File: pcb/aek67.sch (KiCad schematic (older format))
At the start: 20 parts, among them J1 AVR-ISP-6, SW1 SW_PUSH, U1 ATmega32U4-AU, U2 PRTR5V0U2X, X1 XTAL_GND

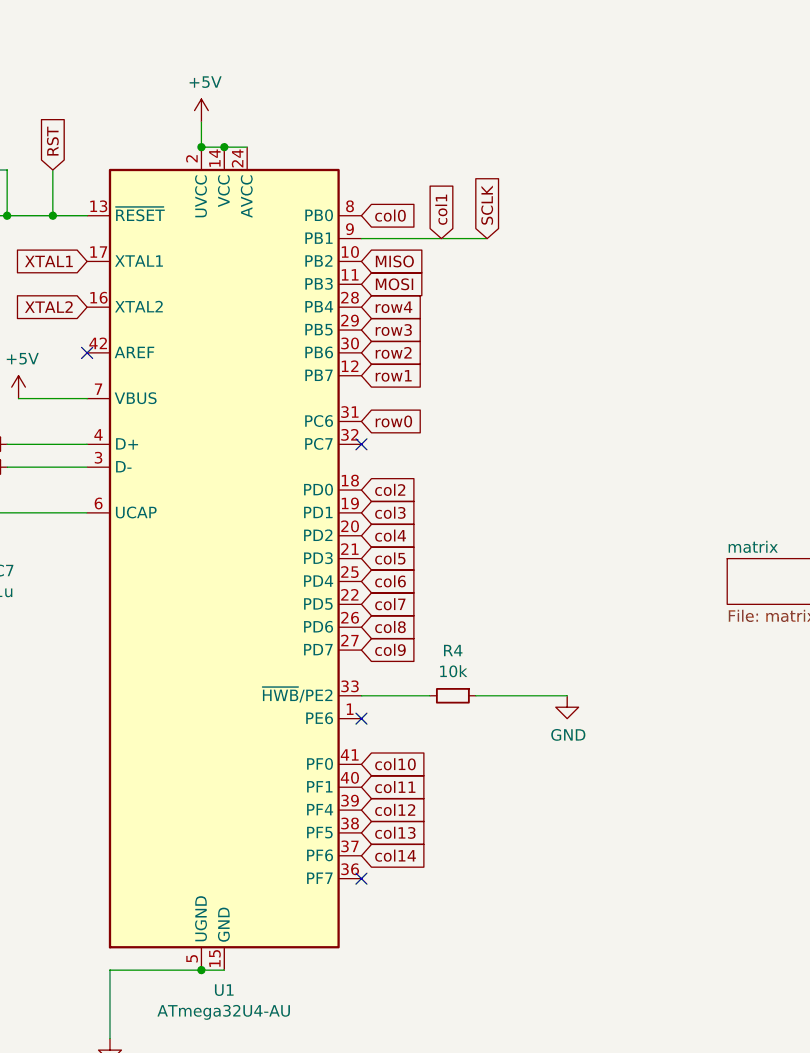
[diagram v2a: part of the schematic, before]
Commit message: reorder rows/cols to MCU pins
to better orient them
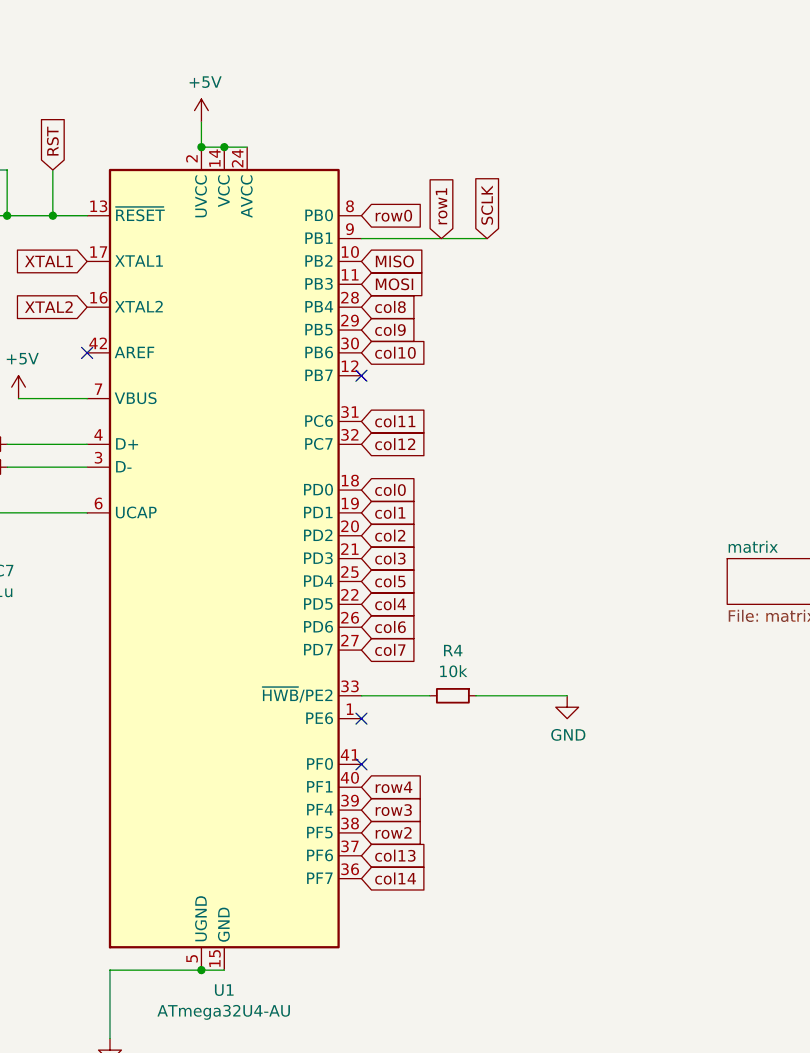
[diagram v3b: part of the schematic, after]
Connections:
- net col0: now also U1.18 (PD0); no longer U1.8 (PB0)
- net col10: now also U1.30 (PB6); no longer U1.41 (PF0)
- net col11: now also U1.31 (PC6); no longer U1.40 (PF1)
- net col12: now also U1.32 (PC7); no longer U1.39 (PF4)
- net col13: now also U1.37 (PF6); no longer U1.38 (PF5)
- net col14: now also U1.36 (PF7); no longer U1.37 (PF6)
- net col2: now also U1.20 (PD2); no longer U1.18 (PD0)
- net col3: now also U1.21 (PD3); no longer U1.19 (PD1)
- net col4: now also U1.22 (PD5); no longer U1.20 (PD2)
- net col5: now also U1.25 (PD4); no longer U1.21 (PD3)
- net col6: now also U1.26 (PD6); no longer U1.25 (PD4)
- net col7: now also U1.27 (PD7); no longer U1.22 (PD5)
- net col8: now also U1.28 (PB4); no longer U1.26 (PD6)
- net col9: now also U1.29 (PB5); no longer U1.27 (PD7)
- net row0: now also U1.8 (PB0); no longer U1.31 (PC6)
- net row2: now also U1.38 (PF5); no longer U1.30 (PB6)
- net row3: now also U1.39 (PF4); no longer U1.29 (PB5)
- net row4: now also U1.40 (PF1); no longer U1.28 (PB4)
- net row1: no longer names the net of U1.12 (PB7)
- new net col1: U1.19 (PD1)
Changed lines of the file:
@@
 $EndSheet
 Text GLabel 7100 3600 2    50   Input ~ 0
+col11
+Text GLabel 7100 3300 2    50   Input ~ 0
+col10
+Text GLabel 7100 3200 2    50   Input ~ 0
+col9
+Text GLabel 7100 3100 2    50   Input ~ 0
+col8
+Text GLabel 7100 3900 2    50   Input ~ 0
+col0
+Text GLabel 7100 4000 2    50   Input ~ 0
+col1
+Text GLabel 7100 4100 2    50   Input ~ 0
+col2
+Text GLabel 7100 4200 2    50   Input ~ 0
+col3
+Text GLabel 7100 4300 2    50   Input ~ 0
+col5
+Text GLabel 7100 4400 2    50   Input ~ 0
+col4
+Text GLabel 7100 4500 2    50   Input ~ 0
+col6
+Text GLabel 7100 4600 2    50   Input ~ 0
+col7
+Text GLabel 7100 5200 2    50   Input ~ 0
+row4
+Text GLabel 7100 5300 2    50   Input ~ 0
+row3
+Text GLabel 7100 5400 2    50   Input ~ 0
+row2
+Text GLabel 7100 5500 2    50   Input ~ 0
+col13
+Text GLabel 7100 2700 2    50   Input ~ 0
 row0
-Text GLabel 7100 3400 2    50   Input ~ 0
-row1
-Text GLabel 7100 3300 2    50   Input ~ 0
-row2
-Text GLabel 7100 3200 2    50   Input ~ 0
-row3
-Text GLabel 7100 3100 2    50   Input ~ 0
-row4
-Text GLabel 7100 3900 2    50   Input ~ 0
-col2
-Text GLabel 7100 4000 2    50   Input ~ 0
-col3
-Text GLabel 7100 4100 2    50   Input ~ 0
-col4
-Text GLabel 7100 4200 2    50   Input ~ 0
-col5
-Text GLabel 7100 4300 2    50   Input ~ 0
-col6
-Text GLabel 7100 4400 2    50   Input ~ 0
-col7
-Text GLabel 7100 4500 2    50   Input ~ 0
-col8
-Text GLabel 7100 4600 2    50   Input ~ 0
-col9
-Text GLabel 7100 5100 2    50   Input ~ 0
-col10
-Text GLabel 7100 5200 2    50   Input ~ 0
-col11
-Text GLabel 7100 5300 2    50   Input ~ 0
-col12
-Text GLabel 7100 5400 2    50   Input ~ 0
-col13
-Text GLabel 7100 5500 2    50   Input ~ 0
-col14
-Text GLabel 7100 2700 2    50   Input ~ 0
-col0
 Wire Wire Line
 	7100 2800 7650 2800
 Text GLabel 7450 2800 1    50   Input ~ 0
-col1
-NoConn ~ 7100 5600
+row1
 NoConn ~ 7100 4900
-NoConn ~ 7100 3700
 $Comp
 L power:GND #PWR09
@@
 	2500 6650 2500 6750
 Connection ~ 2500 6650
+Text GLabel 7100 3700 2    50   Input ~ 0
+col12
+Text GLabel 7100 5600 2    50   Input ~ 0
+col14
+NoConn ~ 7100 5100
+NoConn ~ 7100 3400
 $EndSCHEMATC

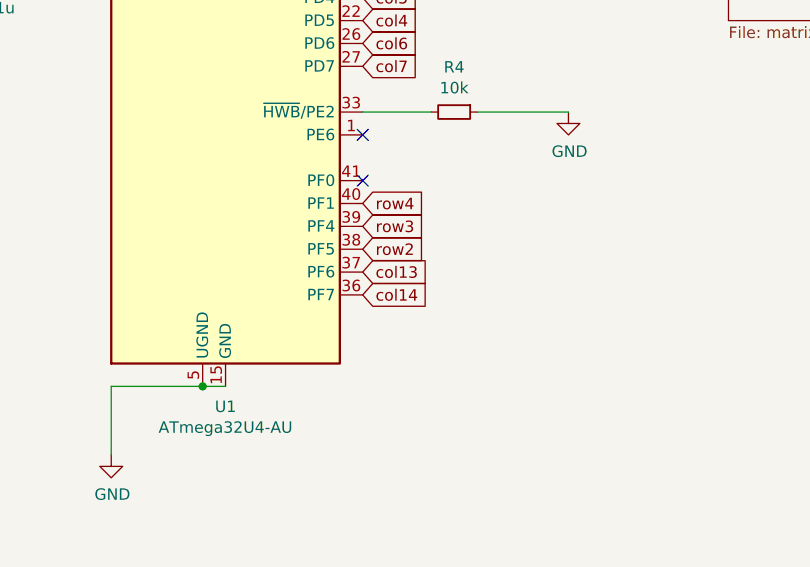
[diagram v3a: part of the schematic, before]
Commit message: routed almost all rows& columns
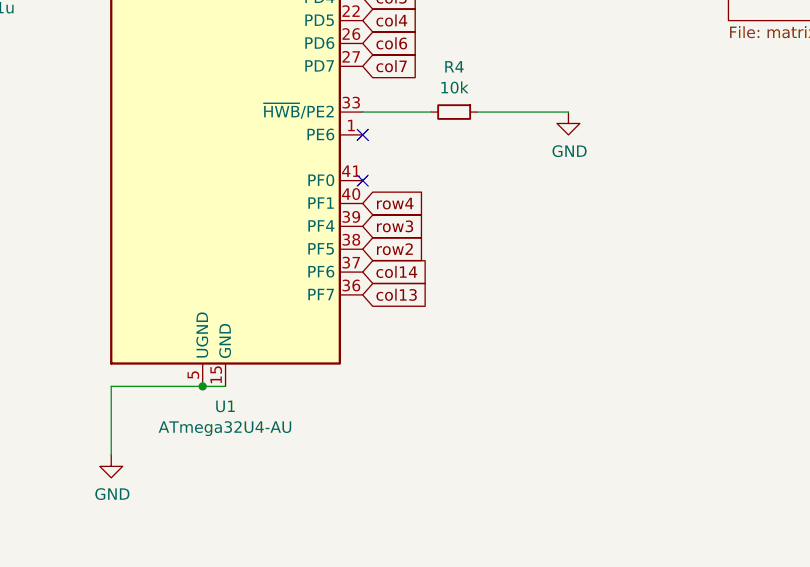
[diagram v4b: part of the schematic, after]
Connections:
- net col13: now also U1.36 (PF7); no longer U1.37 (PF6)
- net col14: now also U1.37 (PF6); no longer U1.36 (PF7)
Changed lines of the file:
@@
 row2
 Text GLabel 7100 5500 2    50   Input ~ 0
-col13
+col14
 Text GLabel 7100 2700 2    50   Input ~ 0
 row0
@@
 col12
 Text GLabel 7100 5600 2    50   Input ~ 0
-col14
+col13
 NoConn ~ 7100 5100
 NoConn ~ 7100 3400

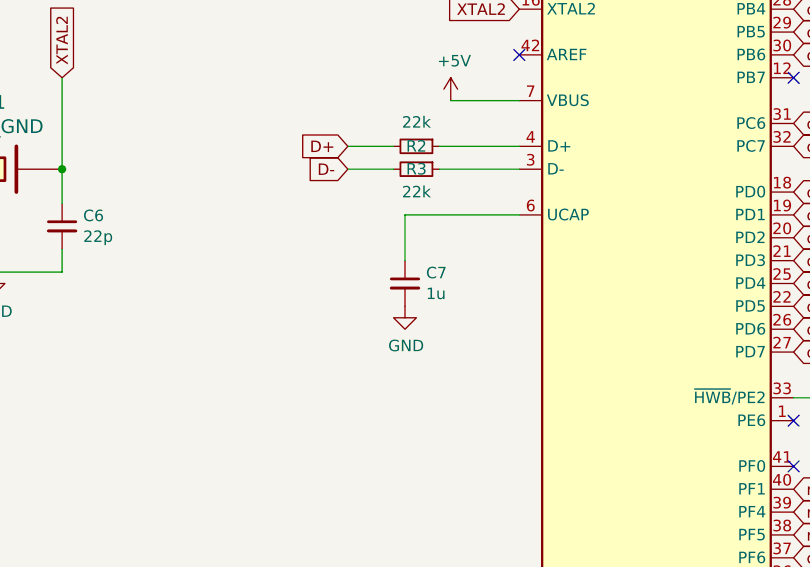
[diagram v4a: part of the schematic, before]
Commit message: Fix footprints of Capacitors
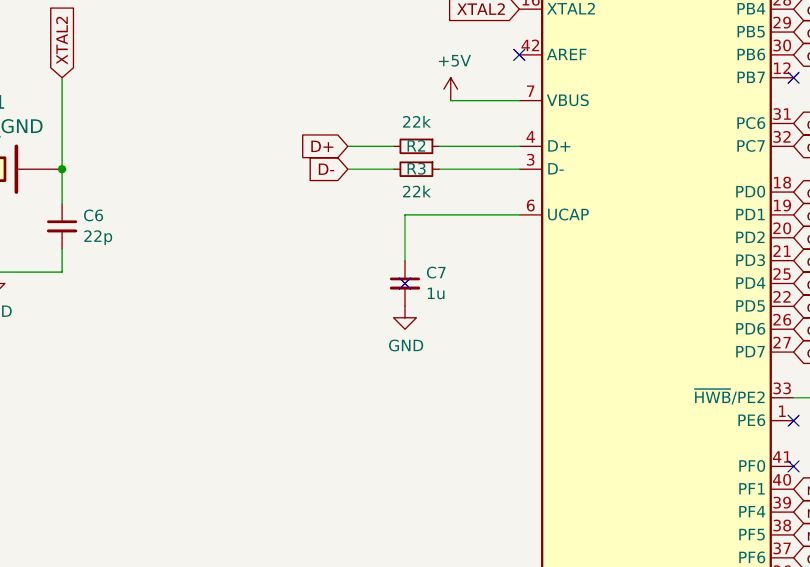
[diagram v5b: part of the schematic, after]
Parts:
- C1, C2, C3, C4, C5, C6, C7: footprint Diode_SMD:D_SOD-123 -> Capacitor_SMD:C_0805_2012Metric_Pad1.15x1.40mm_HandSolder
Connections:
- no-connect marks 6 -> 7
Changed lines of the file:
@@
 F 0 "C1" H 750 1150 50  0000 L CNN
 F 1 "0.1u" H 650 1000 50  0000 L CNN
-F 2 "Diode_SMD:D_SOD-123" H 900 1100 50  0001 C CNN
+F 2 "Capacitor_SMD:C_0805_2012Metric_Pad1.15x1.40mm_HandSolder" H 900 1100 50  0001 C CNN
 F 3 "~" H 900 1100 50  0001 C CNN
 	1    900  1100
@@
 F 0 "C2" H 1050 1150 50  0000 L CNN
 F 1 "0.1u" H 950 1000 50  0000 L CNN
-F 2 "Diode_SMD:D_SOD-123" H 1200 1100 50  0001 C CNN
+F 2 "Capacitor_SMD:C_0805_2012Metric_Pad1.15x1.40mm_HandSolder" H 1200 1100 50  0001 C CNN
 F 3 "~" H 1200 1100 50  0001 C CNN
 	1    1200 1100
@@
 F 0 "C3" H 1650 1150 50  0000 L CNN
 F 1 "0.1u" H 1600 1000 50  0000 L CNN
-F 2 "Diode_SMD:D_SOD-123" H 1600 1100 50  0001 C CNN
+F 2 "Capacitor_SMD:C_0805_2012Metric_Pad1.15x1.40mm_HandSolder" H 1600 1100 50  0001 C CNN
 F 3 "~" H 1600 1100 50  0001 C CNN
 	1    1600 1100
@@
 F 0 "C4" H 1950 1150 50  0000 L CNN
 F 1 "10u" H 1900 1000 50  0000 L CNN
-F 2 "Diode_SMD:D_SOD-123" H 1900 1100 50  0001 C CNN
+F 2 "Capacitor_SMD:C_0805_2012Metric_Pad1.15x1.40mm_HandSolder" H 1900 1100 50  0001 C CNN
 F 3 "~" H 1900 1100 50  0001 C CNN
 	1    1900 1100
@@
 F 0 "C5" H 3100 4100 50  0000 L CNN
 F 1 "22p" H 3100 4000 50  0000 L CNN
-F 2 "Diode_SMD:D_SOD-123" H 3300 4050 50  0001 C CNN
+F 2 "Capacitor_SMD:C_0805_2012Metric_Pad1.15x1.40mm_HandSolder" H 3300 4050 50  0001 C CNN
 F 3 "~" H 3300 4050 50  0001 C CNN
 	1    3300 4050
@@
 F 0 "C6" H 3992 4096 50  0000 L CNN
 F 1 "22p" H 3992 4005 50  0000 L CNN
-F 2 "Diode_SMD:D_SOD-123" H 3900 4050 50  0001 C CNN
+F 2 "Capacitor_SMD:C_0805_2012Metric_Pad1.15x1.40mm_HandSolder" H 3900 4050 50  0001 C CNN
 F 3 "~" H 3900 4050 50  0001 C CNN
 	1    3900 4050
@@
 F 0 "C7" H 5492 4346 50  0000 L CNN
 F 1 "1u" H 5492 4255 50  0000 L CNN
-F 2 "Diode_SMD:D_SOD-123" H 5400 4300 50  0001 C CNN
+F 2 "Capacitor_SMD:C_0805_2012Metric_Pad1.15x1.40mm_HandSolder" H 5400 4300 50  0001 C CNN
 F 3 "~" H 5400 4300 50  0001 C CNN
 	1    5400 4300
@@
 NoConn ~ 7100 5100
 NoConn ~ 7100 3400
+NoConn ~ 5400 4300
 $EndSCHEMATC

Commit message: use the correct crystal footprints
with opposite XTAL pads, in consequence redid the GND zones
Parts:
- X1: symbol keyboard_parts:XTAL_GND -> Device:Crystal_GND24_Small
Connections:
- net GND: now also X1.2, X1.4; no longer X1.3
- net XTAL2: now also X1.3; no longer X1.2
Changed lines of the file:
@@
 XTAL2
 $Comp
-L keyboard_parts:XTAL_GND X1
+L Device:Crystal_GND24_Small X1
 U 1 1 5E165594
 P 3600 3800
@@
 Wire Wire Line
 	3900 3400 3900 3800
-Wire Wire Line
-	3300 3800 3300 3400
-Wire Wire Line
-	3600 4000 3600 4250
 Wire Wire Line
 	3600 4250 3300 4250
@@
 	1    0    0    -1
 $EndComp
-Wire Wire Line
-	3300 3950 3300 3800
-Connection ~ 3300 3800
 Wire Wire Line
 	3300 4150 3300 4250
@@
 NoConn ~ 7100 3400
 NoConn ~ 5400 4300
+Wire Wire Line
+	3700 3800 3900 3800
+Wire Wire Line
+	3300 3400 3300 3800
+Wire Wire Line
+	3500 3800 3300 3800
+Connection ~ 3300 3800
+Wire Wire Line
+	3300 3800 3300 3950
+Wire Wire Line
+	3600 3900 3600 4000
+Wire Wire Line
+	3600 3700 3750 3700
+Wire Wire Line
+	3750 3700 3750 4000
+Wire Wire Line
+	3750 4000 3600 4000
+Connection ~ 3600 4000
+Wire Wire Line
+	3600 4000 3600 4250
 $EndSCHEMATC

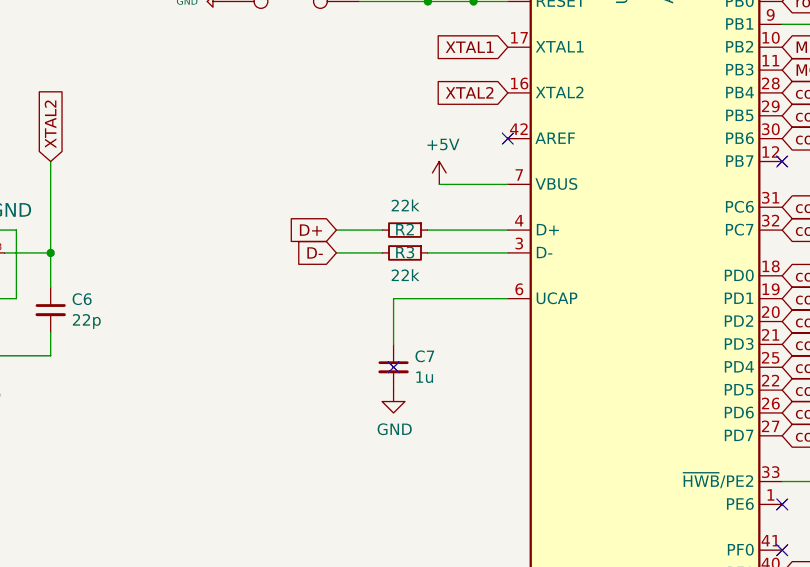
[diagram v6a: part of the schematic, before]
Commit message: turns out it 22ohm, not 22k for D+/D-
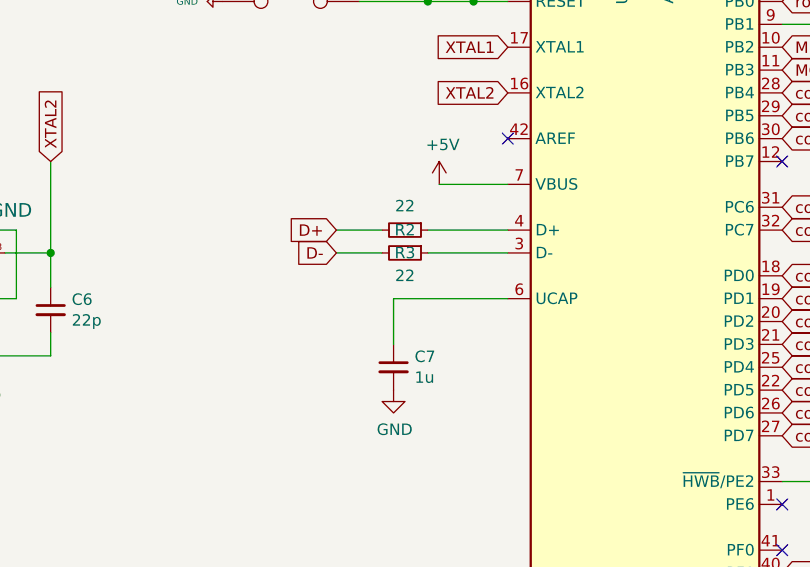
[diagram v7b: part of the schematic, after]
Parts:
- R2, R3: value 22k -> 22
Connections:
- no-connect marks 7 -> 6
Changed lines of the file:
@@
 P 5450 3700
 F 0 "R2" V 5450 3700 50  0000 C CNN
-F 1 "22k" V 5345 3700 50  0000 C CNN
+F 1 "22" V 5345 3700 50  0000 C CNN
 F 2 "Resistor_SMD:R_0805_2012Metric_Pad1.15x1.40mm_HandSolder" H 5450 3700 50  0001 C CNN
 F 3 "~" H 5450 3700 50  0001 C CNN
@@
 P 5450 3800
 F 0 "R3" V 5450 3800 50  0000 C CNN
-F 1 "22k" V 5550 3800 50  0000 C CNN
+F 1 "22" V 5550 3800 50  0000 C CNN
 F 2 "Resistor_SMD:R_0805_2012Metric_Pad1.15x1.40mm_HandSolder" H 5450 3800 50  0001 C CNN
 F 3 "~" H 5450 3800 50  0001 C CNN
@@
 NoConn ~ 7100 5100
 NoConn ~ 7100 3400
-NoConn ~ 5400 4300
 Wire Wire Line
 	3700 3800 3900 3800
